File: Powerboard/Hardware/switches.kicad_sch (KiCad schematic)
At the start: 21 parts, among them J4 Conn_01x02_Male, J5 Conn_01x08_Male, J6 Conn_01x02_Male, Q1 PXP012-30QLJ, Q2 PXP012-30QLJ, Q3 PXP012-30QLJ, Q4 PXP012-30QLJ, U6 LTC4412xS6, U7 LTC4412xS6

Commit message: firmware updates
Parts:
- removed Q1, Q2, Q3, Q4: PXP012-30QLJ, iclr:PXP01230QLJ, symbol iclr:PXP012-30QLJ
- added Q1: SSM3K15AMFV,L3F, Package_TO_SOT_SMD:SOT-723, symbol Device:Q_NMOS_GSD
- added Q10, Q7, Q8, Q9: SQS141ELNW-T1_GE3, iclr:SQS850ENT1_GE3, symbol iclr:SQS141ELNW-T1_GE3
- added R38: 10k, Resistor_SMD:R_0402_1005Metric, symbol Device:R_Small
- added R39: 1k, Resistor_SMD:R_0402_1005Metric, symbol Device:R_Small
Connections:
- net +12V: now also Q9.10 (D_6), Q9.11 (D_7), Q9.5 (D_1), Q9.6 (D_2), Q9.8 (D_4), Q9.9 (D_5), R38.2
- net GND: now also Q1.2 (S), R39.1
- net RBUS_uC_V: now also Q7.10 (D_6), Q7.11 (D_7), Q7.5 (D_1), Q7.6 (D_2), Q7.7 (D_3), Q7.8 (D_4), Q7.9 (D_5)
- net at U6.5 (GATE): now also Q7.4 (G), Q8.4 (G)
- net at C23.1, J5.4 (Pin_4), R7.2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: now also Q8.10 (D_6), Q8.11 (D_7), Q8.5 (D_1), Q8.6 (D_2), Q8.7 (D_3), Q8.8 (D_4), Q8.9 (D_5)
- net at C24.1, J5.5 (Pin_5), J5.6 (Pin_6)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: now also Q10.10 (D_6), Q10.11 (D_7), Q10.5 (D_1), Q10.6 (D_2), Q10.7 (D_3), Q10.8 (D_4), Q10.9 (D_5)
- net at U7.5 (GATE): now also Q10.4 (G), Q9.4 (G)
- new net: Q10.1 (S_1), Q10.2 (S_2), Q10.3 (S_3), Q9.1 (S_1), Q9.2 (S_2), Q9.3 (S_3)
- new net: Q7.1 (S_1), Q7.2 (S_2), Q7.3 (S_3), Q8.1 (S_1), Q8.2 (S_2), Q8.3 (S_3)
- new net BUCK_EN: Q1.1 (G), R39.2
- new net CTL: Q1.3 (D), R38.1

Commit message: v2.1
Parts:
- removed JP3: SolderJumper_2_Bridged, Jumper:SolderJumper-2_P1.3mm_Bridged_RoundedPad1.0x1.5mm, symbol Jumper:SolderJumper_2_Bridged
- removed R19: 10k, Resistor_SMD:R_0402_1005Metric, symbol Device:R_Small
- added JP1: SolderJumper_2_Bridged, Jumper:SolderJumper-2_P1.3mm_Bridged_RoundedPad1.0x1.5mm, symbol Jumper:SolderJumper_2_Bridged
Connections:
- net BUCK_EN is gone; now on an unnamed net: Q1.1 (G), R39.2
- net +12V: now also Q9.7 (D_3)
- net +3V3: now also J6.2 (Pin_2)
- net CTL: now also U7.3 (CTL)
- net DEP_SWITCH: now also JP1.1 (A)
- net GND: no longer J6.2 (Pin_2)
- net at J6.1 (Pin_1): now also JP1.2 (B); no longer U7.3 (CTL)
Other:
- moved on the sheet: J6, Q1, R38, R39

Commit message: can hardware fix, firmware updates
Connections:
- net CAN+: now also J5.7 (Pin_7); no longer J5.8 (Pin_8)
- net CAN-: now also J5.8 (Pin_8); no longer J5.7 (Pin_7)
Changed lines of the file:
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@@
     )
   )
-  (hierarchical_label "CAN+" (shape bidirectional) (at 148.082 155.448 90) (fields_autoplaced)
+  (hierarchical_label "CAN+" (shape bidirectional) (at 145.542 155.448 90) (fields_autoplaced)
     (effects (font (size 1.27 1.27)) (justify left))
   )
@@
     (effects (font (size 1.27 1.27)) (justify left))
   )
-  (hierarchical_label "CAN-" (shape bidirectional) (at 145.542 155.448 90) (fields_autoplaced)
+  (hierarchical_label "CAN-" (shape bidirectional) (at 148.082 155.448 90) (fields_autoplaced)
     (effects (font (size 1.27 1.27)) (justify left))
   )

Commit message: v2.1 ordering
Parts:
- 12VLED1: value DEP_LED -> RED_LED
- 3V3LED1: value LOGIC_LED -> BLUE_LED
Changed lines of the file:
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@@
       (effects (font (size 1.27 1.27)))
     )
-    (property "Value" "LOGIC_LED" (at 89.662 139.0396 0)
+    (property "Value" "BLUE_LED" (at 89.662 139.0396 0)
       (effects (font (size 1.27 1.27)))
     )
@@
       (effects (font (size 1.27 1.27)))
     )
-    (property "Value" "DEP_LED" (at 151.13 131.7244 0)
+    (property "Value" "RED_LED" (at 151.13 131.7244 0)
       (effects (font (size 1.27 1.27)))
     )

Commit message: v2.2 hardware
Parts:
- added J2: FAN, Connector_PinHeader_2.54mm:PinHeader_1x02_P2.54mm_Vertical, symbol Connector:Conn_01x02_Pin
- added R24: 10k, Resistor_SMD:R_0402_1005Metric, symbol Device:R_Small
- added R26: 160k, Resistor_SMD:R_0402_1005Metric, symbol Device:R_Small
- renumbered 12VLED1 to DEPLED1, 3V3LED1 to LOGICLED1, R9 to R27, R14 to R28, R22 to R32, R7 to R33
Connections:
- net GND: now also J2.2 (Pin_2), R26.2
- net at C23.1, J5.4 (Pin_4), Q8.10 (D_6)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: now also J2.1 (Pin_1), R24.1
- net DEP_SWITCH renamed DepSwitch
- net LOGIC_SWITCH renamed LogicSwitch
- new net LogicVoltage: R24.2, R26.1
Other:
- moved on the sheet: C23, C24, DEPLED1, LOGICLED1, R27, R33

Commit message: commit before trying to squish the layout
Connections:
- net GND: now also J2.1 (Pin_1), J4.1 (Pin_1); no longer J2.2 (Pin_2), J4.2 (Pin_2)
- net at JP2.1 (A), R18.2, U6.3 (CTL): now also J4.2 (Pin_2); no longer J4.1 (Pin_1)
- net at C23.1, J5.4 (Pin_4), Q8.10 (D_6)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: no longer J2.1 (Pin_1)
- net at C24.1, J5.5 (Pin_5), J5.6 (Pin_6)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: now also J2.2 (Pin_2)
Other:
- moved on the sheet: J2, J4
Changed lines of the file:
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@@
 	)
 	(junction
+		(at 140.462 141.478)
+		(diameter 0)
+		(color 0 0 0 0)
+	)
+	(junction
 		(at 104.902 111.506)
 		(diameter 0)
@@
 	)
 	(junction
-		(at 137.922 146.05)
-		(diameter 0)
-		(color 0 0 0 0)
-	)
-	(junction
 		(at 196.596 58.42)
 		(diameter 0)
@@
 	(wire
 		(pts
-			(xy 137.922 146.05) (xy 137.922 155.448)
-		)
-		(stroke
-			(width 0)
-			(type default)
-		)
-	)
-	(wire
-		(pts
 			(xy 201.422 83.82) (xy 201.422 58.42)
 		)
@@
 	(wire
 		(pts
+			(xy 140.462 141.478) (xy 144.78 141.478)
+		)
+		(stroke
+			(width 0)
+			(type default)
+		)
+	)
+	(wire
+		(pts
 			(xy 75.692 88.646) (xy 75.819 51.435)
 		)
@@
 	(wire
 		(pts
-			(xy 137.922 119.634) (xy 137.922 146.05)
+			(xy 137.922 119.634) (xy 137.922 155.448)
 		)
 		(stroke
@@
 	(wire
 		(pts
-			(xy 129.794 146.05) (xy 137.922 146.05)
+			(xy 140.462 141.478) (xy 140.462 146.05)
 		)
 		(stroke
@@
 	(wire
 		(pts
-			(xy 140.462 119.634) (xy 140.462 146.05)
+			(xy 140.462 119.634) (xy 140.462 141.478)
 		)
 		(stroke
@@
 	(symbol
 		(lib_id "Connector:Conn_01x02_Male")
-		(at 66.548 80.01 270)
+		(at 64.008 90.17 90)
 		(unit 1)
 		(exclude_from_sim no)
@@
 		(dnp no)
 		(property "Reference" "J4"
-			(at 73.66 84.328 90)
+			(at 64.008 81.026 90)
 			(effects
 				(font
@@
 		)
 		(property "Value" "Conn_01x02_Male"
-			(at 67.818 82.296 90)
+			(at 69.85 83.058 90)
 			(effects
 				(font
@@
 		)
 		(property "Footprint" "Connector_PinHeader_2.54mm:PinHeader_1x02_P2.54mm_Vertical"
-			(at 66.548 80.01 0)
+			(at 64.008 90.17 0)
 			(effects
 				(font
@@
 		)
 		(property "Datasheet" "~"
-			(at 66.548 80.01 0)
+			(at 64.008 90.17 0)
 			(effects
 				(font
@@
 		)
 		(property "Description" ""
-			(at 66.548 80.01 0)
+			(at 64.008 90.17 0)
 			(effects
 				(font
@@
 	(symbol
 		(lib_id "Connector:Conn_01x02_Pin")
-		(at 129.794 140.97 270)
+		(at 147.32 136.398 270)
 		(unit 1)
 		(exclude_from_sim no)
@@
 		(dnp no)
 		(property "Reference" "J2"
-			(at 131.064 147.828 90)
+			(at 148.59 143.256 90)
 			(effects
 				(font
@@
 		)
 		(property "Value" "FAN"
-			(at 131.064 149.749 90)
+			(at 148.59 145.177 90)
 			(effects
 				(font
@@
 		)
 		(property "Footprint" "Connector_PinHeader_2.54mm:PinHeader_1x02_P2.54mm_Vertical"
-			(at 129.794 140.97 0)
+			(at 147.32 136.398 0)
 			(effects
 				(font
@@
 		)
 		(property "Datasheet" "~"
-			(at 129.794 140.97 0)
+			(at 147.32 136.398 0)
 			(effects
 				(font
@@
 		)
 		(property "Description" ""
-			(at 129.794 140.97 0)
+			(at 147.32 136.398 0)
 			(effects
 				(font
@@
 		(lib_name "GND_1")
 		(lib_id "power:GND")
-		(at 127.254 146.05 0)
+		(at 147.32 141.478 0)
 		(unit 1)
 		(exclude_from_sim no)
@@
 		(fields_autoplaced yes)
 		(property "Reference" "#PWR011"
-			(at 127.254 152.4 0)
+			(at 147.32 147.828 0)
 			(effects
 				(font
@@
 		)
 		(property "Value" "GND"
-			(at 127.254 150.1855 0)
+			(at 147.32 145.6135 0)
 			(effects
 				(font
@@
 		)
 		(property "Footprint" ""
-			(at 127.254 146.05 0)
+			(at 147.32 141.478 0)
 			(effects
 				(font
@@
 		)
 		(property "Datasheet" ""
-			(at 127.254 146.05 0)
+			(at 147.32 141.478 0)
 			(effects
 				(font
@@
 		)
 		(property "Description" ""
-			(at 127.254 146.05 0)
+			(at 147.32 141.478 0)
 			(effects
 				(font
@@
 		(dnp no)
 		(property "Reference" "J6"
-			(at 242.316 25.654 90)
+			(at 242.57 25.908 90)
 			(effects
 				(font
@@
 		)
 		(property "Value" "Conn_01x02_Male"
-			(at 236.474 23.622 90)
+			(at 236.728 23.876 90)
 			(effects
 				(font

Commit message: shiven layout change
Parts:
- added C21: 4.7nF, Capacitor_SMD:C_0402_1005Metric, symbol Device:C_Small
- added C22: 10nF, Capacitor_SMD:C_0402_1005Metric, symbol Device:C_Small
- added C26, C27: 0.1uF, Capacitor_SMD:C_0402_1005Metric, symbol Device:C_Small
- added IC1: TPS259830ONRGER, iclr:TPS259830ONRGER, symbol iclr:TPS259830ONRGER
- added R38: 82, Capacitor_SMD:C_0402_1005Metric, symbol Device:R_Small
- added R39: 1M, Capacitor_SMD:C_0402_1005Metric, symbol Device:R_Small
- added R40: 732k, Capacitor_SMD:C_0402_1005Metric, symbol Device:R_Small
- added R41: 73.2k, Capacitor_SMD:C_0402_1005Metric, symbol Device:R_Small
- added R42: 681, Capacitor_SMD:C_0402_1005Metric, symbol Device:R_Small
- added R43: 100k, Capacitor_SMD:C_0402_1005Metric, symbol Device:R_Small
- R24: value 10k -> 2.87k
- R26: value 160k -> 10k
- R28: value 47k -> 97.6
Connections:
- net +3V3: now also R43.1
- net DepVoltage: now also C27.2
- net GND: now also C21.1, C22.1, IC1.11 (NRETRY), IC1.14 (GND_3), IC1.26 (GND_4), IC1.4 (GND_1), IC1.5 (GND_2), R38.2, R41.2, R42.2
- net LogicVoltage: now also C26.2
- net at C23.1, J5.4 (Pin_4), Q8.10 (D_6)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: now also C26.1
- net EFuse_IN: now reaches Q10.10 (D_6), Q10.11 (D_7), Q10.5 (D_1), Q10.6 (D_2), Q10.7 (D_3), Q10.8 (D_4), Q10.9 (D_5), U7.6 (SENSE)
- net EFuse_IN: now also C22.2, IC1.1 (IN_1), IC1.16 (IN_4), IC1.2 (IN_2), IC1.25 (IN_5), IC1.3 (IN_3), R39.1; no longer C24.1, J2.2 (Pin_2), J5.5 (Pin_5), J5.6 (Pin_6), R27.1, R28.1
- new net: IC1.8 (ILIM), R38.1
- new net: C21.2, IC1.7 (ITIMER)
- new net: IC1.6 (EN/UVLO), R39.2, R40.1
- new net DepCurrent: IC1.9 (IMON), R42.1
- new net EFuse_OUT: C24.1, C27.1, IC1.17 (OUT_1), IC1.18 (OUT_2), IC1.19 (OUT_3), IC1.20 (OUT_4), IC1.21 (OUT_5), IC1.22 (OUT_6), IC1.23 (OUT_7), IC1.24 (OUT_8), J2.2 (Pin_2), J5.5 (Pin_5), J5.6 (Pin_6), R27.1, R28.1
- new net EFuse_PG: IC1.13 (PG), R43.2
- new net OVLO: IC1.12 (OVLO), R40.2, R41.1
- no-connect marks 2 -> 4
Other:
- note added: "UV set to 2.7V OV set to 30V"
- note added: "dvdt pin left floating for fastest turn on time"
- moved on the sheet: C23, C24, DEPLED1, J2, J4, J5, J6, JP1, JP2, LOGICLED1, Q1, Q10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

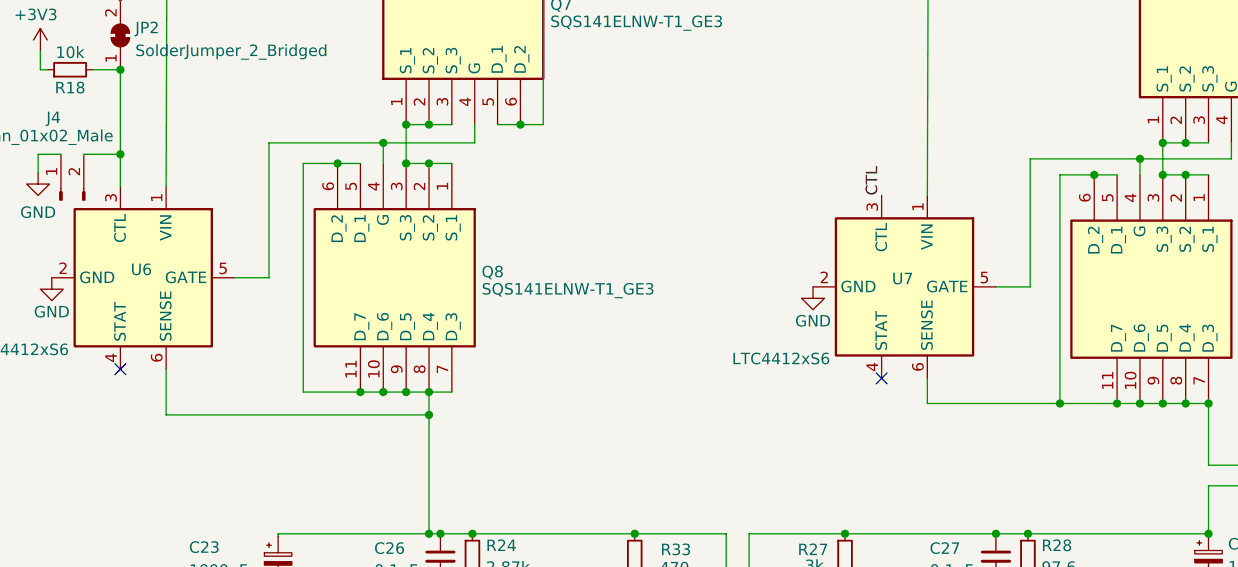
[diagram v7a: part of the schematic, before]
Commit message: added rc on gates, post kiran review
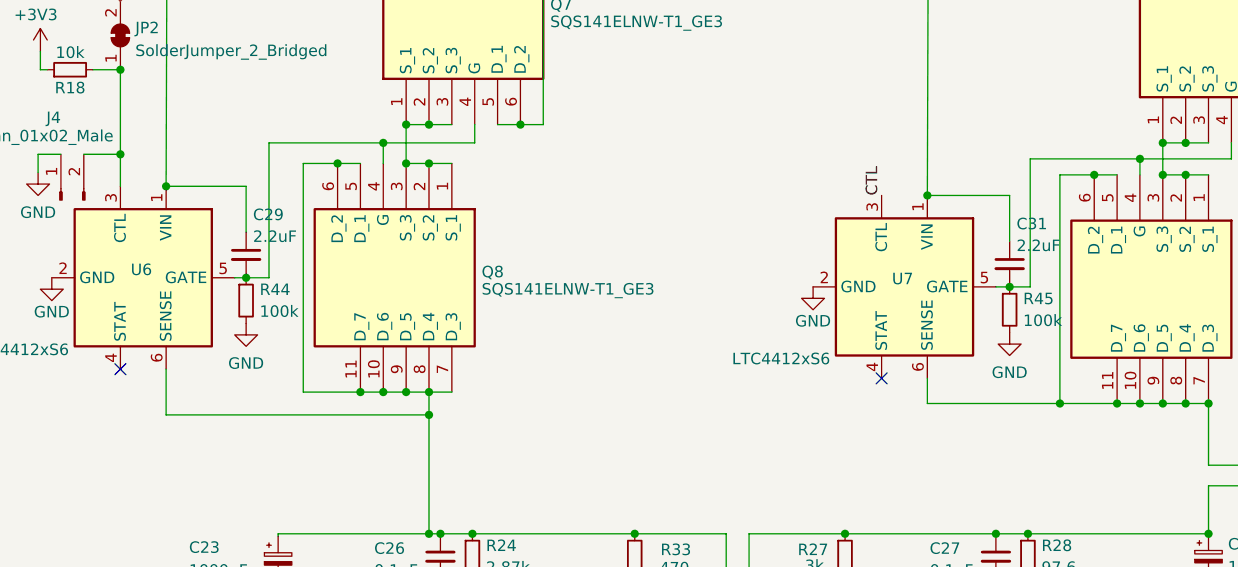
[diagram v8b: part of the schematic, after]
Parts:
- added C29: 2.2uF, Capacitor_SMD:C_0402_1005Metric, symbol Device:C_Small
- added C31: 2.2uF, Capacitor_SMD:C_0805_2012Metric, symbol Device:C_Small
- added R44, R45: 100k, Resistor_SMD:R_0402_1005Metric, symbol Device:R_Small
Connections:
- net +12V: now also C31.1
- net GND: now also R44.2, R45.2
- net RBUS_uC_V: now also C29.1
- net at Q7.4 (G), Q8.4 (G), U6.5 (GATE): now also C29.2, R44.1
- net at Q10.4 (G), Q9.4 (G), U7.5 (GATE): now also C31.2, R45.1
